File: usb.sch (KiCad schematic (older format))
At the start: 7 parts, among them U23 FT313HL-LQFP64-0.5

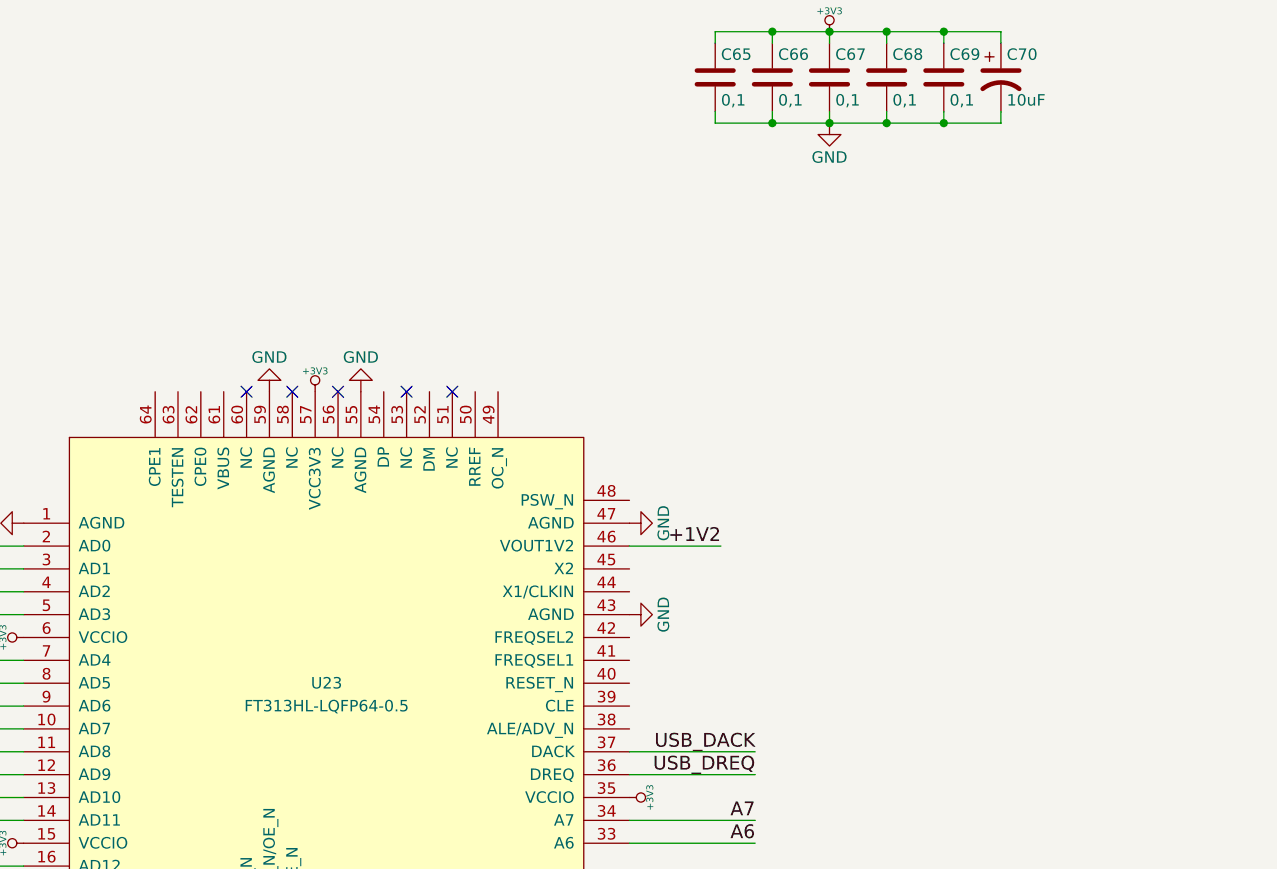
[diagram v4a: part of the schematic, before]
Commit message: Add USB connector
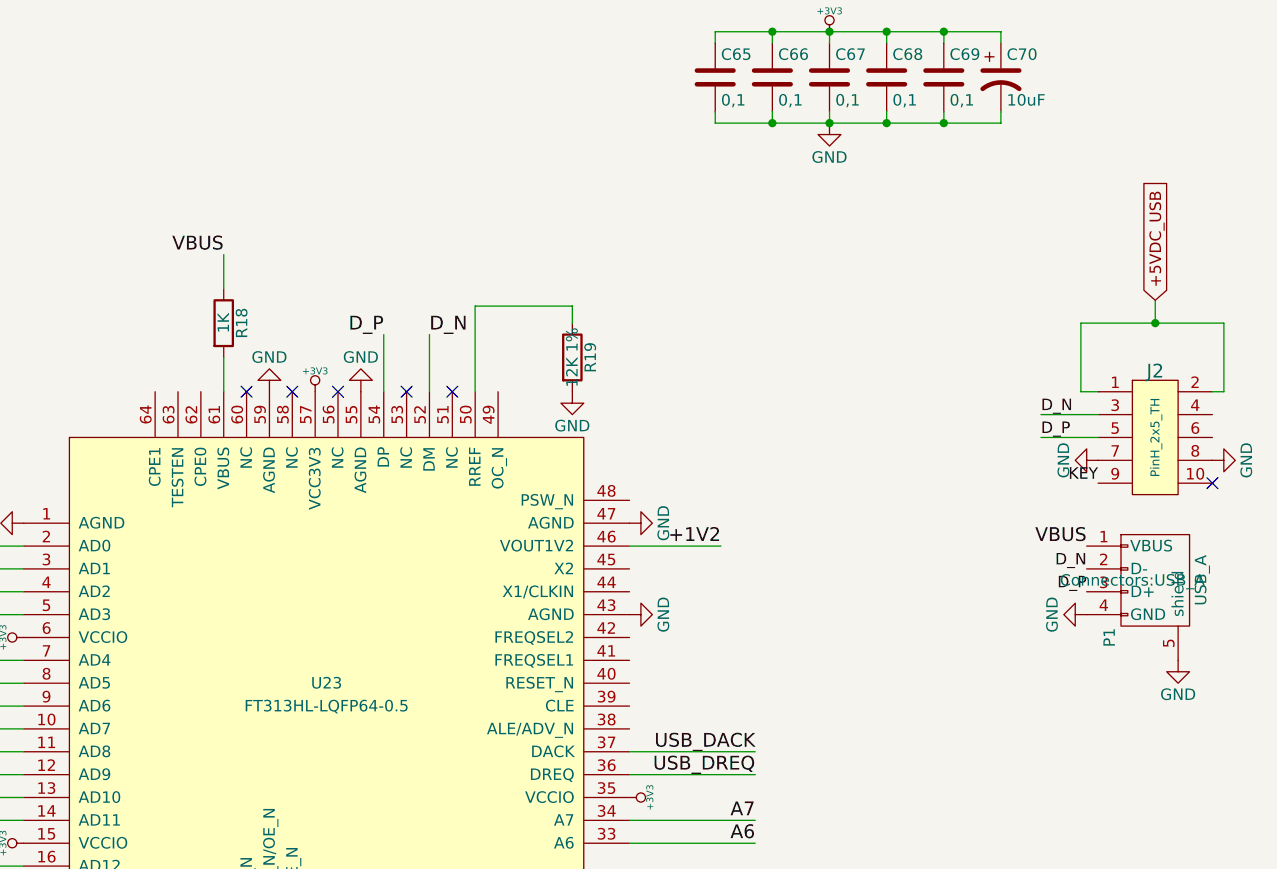
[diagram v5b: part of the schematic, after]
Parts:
- added J2: Pinheader_2x5_TH_WALL, Pin_Headers:Pin_Header_Straight_2x05_Pitch2.54mm, symbol Pinheader_2x5_TH_WALL
- added P1: USB_A, Connectors:USB_A, symbol USB_A
- added R18: 1K, symbol R
- added R19: 12K 1%, symbol R
- C65, C66, C67, C68, C69: footprint (none) -> Capacitors_SMD:C_0603
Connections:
- net labels added: +5VDC_USB, D_N, D_P, KEY, VBUS
- wire segments 77 -> 92
- no-connect marks 5 -> 6
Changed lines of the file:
@@
 $EndComp
 $Comp
-L GND #PWR147
+L GND #PWR148
 U 1 1 587F942A
 P 7000 3425
-F 0 "#PWR147" H 7000 3175 50  0001 C CNN
+F 0 "#PWR148" H 7000 3175 50  0001 C CNN
 F 1 "GND" H 7000 3275 50  0000 C CNN
 F 2 "" H 7000 3425 50  0000 C CNN
@@
 $EndComp
 $Comp
-L GND #PWR146
+L GND #PWR147
 U 1 1 587F944F
 P 7000 3025
-F 0 "#PWR146" H 7000 2775 50  0001 C CNN
+F 0 "#PWR147" H 7000 2775 50  0001 C CNN
 F 1 "GND" H 7000 2875 50  0000 C CNN
 F 2 "" H 7000 3025 50  0000 C CNN
@@
 $EndComp
 $Comp
-L +3V3 #PWR149
+L +3V3 #PWR150
 U 1 1 587FA4A0
 P 7875 875
-F 0 "#PWR149" H 7975 925 20  0001 C CNN
+F 0 "#PWR150" H 7975 925 20  0001 C CNN
 F 1 "+3V3" H 7875 965 30  0000 C CNN
 F 2 "" H 7875 875 60  0000 C CNN
@@
 F 0 "C65" H 7400 1175 50  0000 L CNN
 F 1 "0,1" H 7400 975 50  0000 L CNN
-F 2 "" H 7413 925 50  0001 C CNN
+F 2 "Capacitors_SMD:C_0603" H 7413 925 50  0001 C CNN
 F 3 "" H 7375 1075 50  0000 C CNN
 	1    7375 1075
@@
 F 0 "C66" H 7650 1175 50  0000 L CNN
 F 1 "0,1" H 7650 975 50  0000 L CNN
-F 2 "" H 7663 925 50  0001 C CNN
+F 2 "Capacitors_SMD:C_0603" H 7663 925 50  0001 C CNN
 F 3 "" H 7625 1075 50  0000 C CNN
 	1    7625 1075
@@
 F 0 "C67" H 7900 1175 50  0000 L CNN
 F 1 "0,1" H 7900 975 50  0000 L CNN
-F 2 "" H 7913 925 50  0001 C CNN
+F 2 "Capacitors_SMD:C_0603" H 7913 925 50  0001 C CNN
 F 3 "" H 7875 1075 50  0000 C CNN
 	1    7875 1075
@@
 F 0 "C68" H 8150 1175 50  0000 L CNN
 F 1 "0,1" H 8150 975 50  0000 L CNN
-F 2 "" H 8163 925 50  0001 C CNN
+F 2 "Capacitors_SMD:C_0603" H 8163 925 50  0001 C CNN
 F 3 "" H 8125 1075 50  0000 C CNN
 	1    8125 1075
@@
 $EndComp
 $Comp
-L GND #PWR150
+L GND #PWR151
 U 1 1 587FA6CC
 P 7875 1275
-F 0 "#PWR150" H 7875 1025 50  0001 C CNN
+F 0 "#PWR151" H 7875 1025 50  0001 C CNN
 F 1 "GND" H 7875 1125 50  0000 C CNN
 F 2 "" H 7875 1275 50  0000 C CNN
@@
 $EndComp
 $Comp
-L +3V3 #PWR148
+L +3V3 #PWR149
 U 1 1 587FB222
 P 7000 4225
-F 0 "#PWR148" H 7100 4275 20  0001 C CNN
+F 0 "#PWR149" H 7100 4275 20  0001 C CNN
 F 1 "+3V3" H 7000 4315 30  0000 C CNN
 F 2 "" H 7000 4225 60  0000 C CNN
@@
 F 0 "C69" H 8400 1175 50  0000 L CNN
 F 1 "0,1" H 8400 975 50  0000 L CNN
-F 2 "" H 8413 925 50  0001 C CNN
+F 2 "Capacitors_SMD:C_0603" H 8413 925 50  0001 C CNN
 F 3 "" H 8375 1075 50  0000 C CNN
 	1    8375 1075
@@
 Text HLabel 1575 5325 0    60   BiDi ~ 0
 USB_DREQ
+$Comp
+L Pinheader_2x5_TH_WALL J2
+U 1 1 588FAD1B
+P 9300 2800
+F 0 "J2" H 9300 3240 60  0000 C CNN
+F 1 "Pinheader_2x5_TH_WALL" H 9270 3330 60  0001 C CNN
+F 2 "Pin_Headers:Pin_Header_Straight_2x05_Pitch2.54mm" H 9280 3430 60  0001 C CNN
+F 3 "" H 9300 2900 60  0000 C CNN
+F 4 "S9169-ND" H 9320 3900 60  0001 C CNN "Vendor Part Number"
+F 5 "SBH11-PBPC-D05-ST-BK" H 9250 3610 60  0001 C CNN "Manufacturer Part Number"
+F 6 "CONN HEADER, 2.54MM, 10POS, GOLD," H 9350 3520 60  0001 C CNN "Description"
+F 7 "Digi-Key" H 9280 3800 60  0001 C CNN "Vendor"
+F 8 "Sullins Connector Solutions" H 9260 3710 60  0001 C CNN "Manufacturer"
+F 9 "PinH_2x5_TH" V 9300 2950 39  0000 C CNN "Component Value"
+	1    9300 2800
+	1    0    0    -1
+$EndComp
+$Comp
+L GND #PWR155
+U 1 1 588FAE50
+P 9550 2750
+F 0 "#PWR155" H 9550 2500 50  0001 C CNN
+F 1 "GND" H 9550 2600 50  0000 C CNN
+F 2 "" H 9550 2750 50  0000 C CNN
+F 3 "" H 9550 2750 50  0000 C CNN
+	1    9550 2750
+	0    -1   -1   0
+$EndComp
+$Comp
+L GND #PWR153
+U 1 1 588FAEAB
+P 9050 2750
+F 0 "#PWR153" H 9050 2500 50  0001 C CNN
+F 1 "GND" H 9050 2600 50  0000 C CNN
+F 2 "" H 9050 2750 50  0000 C CNN
+F 3 "" H 9050 2750 50  0000 C CNN
+	1    9050 2750
+	0    1    1    0
+$EndComp
+NoConn ~ 9550 2850
+Text Label 9050 2850 2    50   ~ 0
+KEY
+Text GLabel 9300 2050 1    50   Input ~ 0
++5VDC_USB
+Wire Wire Line
+	9300 2050 9300 2150
+Wire Wire Line
+	8975 2150 9600 2150
+Wire Wire Line
+	8975 2150 8975 2450
+Wire Wire Line
+	8975 2450 9050 2450
+Wire Wire Line
+	9600 2150 9600 2450
+Wire Wire Line
+	9600 2450 9550 2450
+Connection ~ 9300 2150
+Wire Wire Line
+	9050 2550 8800 2550
+Wire Wire Line
+	9050 2650 8800 2650
+Text Label 8800 2550 0    50   ~ 0
+D_N
+Text Label 8800 2650 0    50   ~ 0
+D_P
+Wire Wire Line
+	5925 2450 5925 2200
+Wire Wire Line
+	6125 2450 6125 2200
+Text Label 5925 2200 2    60   ~ 0
+D_P
+Text Label 6125 2200 0    60   ~ 0
+D_N
+$Comp
+L R R19
+U 1 1 588FBE83
+P 6750 2300
+F 0 "R19" V 6830 2300 50  0000 C CNN
+F 1 "12K 1%" V 6750 2300 50  0000 C CNN
+F 2 "" V 6680 2300 50  0000 C CNN
+F 3 "" H 6750 2300 50  0000 C CNN
+	1    6750 2300
+	1    0    0    -1
+$EndComp
+Wire Wire Line
+	6325 2450 6325 2075
+Wire Wire Line
+	6325 2075 6750 2075
+Wire Wire Line
+	6750 2075 6750 2150
+$Comp
+L GND #PWR146
+U 1 1 588FBF68
+P 6750 2450
+F 0 "#PWR146" H 6750 2200 50  0001 C CNN
+F 1 "GND" H 6750 2300 50  0000 C CNN
+F 2 "" H 6750 2450 50  0000 C CNN
+F 3 "" H 6750 2450 50  0000 C CNN
+	1    6750 2450
+	1    0    0    -1
+$EndComp
+$Comp
+L R R18
+U 1 1 588FC74E
+P 5225 2150
+F 0 "R18" V 5305 2150 50  0000 C CNN
+F 1 "1K" V 5225 2150 50  0000 C CNN
+F 2 "" V 5155 2150 50  0000 C CNN
+F 3 "" H 5225 2150 50  0000 C CNN
+	1    5225 2150
+	1    0    0    -1
+$EndComp
+Wire Wire Line
+	5225 2300 5225 2450
+Wire Wire Line
+	5225 2000 5225 1850
+Text Label 5225 1850 2    60   ~ 0
+VBUS
+$Comp
+L USB_A P1
+U 1 1 588FD24C
+P 9300 3325
+F 0 "P1" H 9500 3125 50  0000 C CNN
+F 1 "USB_A" H 9250 3525 50  0000 C CNN
+F 2 "Connectors:USB_A" V 9250 3225 50  0000 C CNN
+F 3 "" V 9250 3225 50  0000 C CNN
+	1    9300 3325
+	0    1    1    0
+$EndComp
+Text Label 9000 3125 2    60   ~ 0
+VBUS
+Text Label 9000 3225 2    50   ~ 0
+D_N
+Text Label 9000 3325 2    50   ~ 0
+D_P
+$Comp
+L GND #PWR152
+U 1 1 588FD418
+P 9000 3425
+F 0 "#PWR152" H 9000 3175 50  0001 C CNN
+F 1 "GND" H 9000 3275 50  0000 C CNN
+F 2 "" H 9000 3425 50  0000 C CNN
+F 3 "" H 9000 3425 50  0000 C CNN
+	1    9000 3425
+	0    1    1    0
+$EndComp
+$Comp
+L GND #PWR154
+U 1 1 588FDBE9
+P 9400 3625
+F 0 "#PWR154" H 9400 3375 50  0001 C CNN
+F 1 "GND" H 9400 3475 50  0000 C CNN
+F 2 "" H 9400 3625 50  0000 C CNN
+F 3 "" H 9400 3625 50  0000 C CNN
+	1    9400 3625
+	1    0    0    -1
+$EndComp
 $EndSCHEMATC

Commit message: More USB stuff
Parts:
- removed J2: Pinheader_2x5_TH_WALL, Pin_Headers:Pin_Header_Straight_2x05_Pitch2.54mm, symbol Pinheader_2x5_TH_WALL
- added C108: 0,1, Capacitors_SMD:C_0603, symbol C
- added C109: 22uF, Capacitors_Tantalum_SMD:CP_Tantalum_Case-B_EIA-3528-21_Wave, symbol CP1
- added C110, C111: 27pF, Capacitors_SMD:C_0603, symbol C
- added R20, R22, R23, R25: 000, Resistors_SMD:R_0603, symbol R
- added R21, R24: 10K, Resistors_SMD:R_0603, symbol R
- added U25: TPS2024D, Housings_SOIC:SOIC-8_3.9x4.9mm_Pitch1.27mm, symbol TPS2024D
- added Y2: Geyer_KX7_12MHz, Crystals:Crystal_SMD_3225-4pin_3.2x2.5mm, symbol Crystal_GND24
- R18, R19: footprint (none) -> Resistors_SMD:R_0603
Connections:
- net labels added: +5VDC, CPE0, CPE1, OC_N, USB_NRESET, nEN
- net labels removed: +5VDC_USB, KEY
- wire segments 92 -> 121
- no-connect marks 6 -> 5
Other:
- note added: "TESTEN: internal pulldown.\nFor normal operation leave floating."
- moved on the sheet: C65, C66, C67, C68, C69, C70, P1

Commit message: Up
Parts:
- added C112, C113, C114: 0,1, Capacitors_SMD:C_0603, symbol C
- added C115: 10uF, symbol CP1
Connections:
- wire segments 121 -> 131
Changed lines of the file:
@@
 NoConn ~ 5325 2450
 $Comp
-L GND #PWR139
+L GND #PWR152
 U 1 1 587F93F7
 P 4350 3025
-F 0 "#PWR139" H 4350 2775 50  0001 C CNN
+F 0 "#PWR152" H 4350 2775 50  0001 C CNN
 F 1 "GND" H 4350 2875 50  0000 C CNN
 F 2 "" H 4350 3025 50  0000 C CNN
@@
 $EndComp
 $Comp
-L GND #PWR148
+L GND #PWR157
 U 1 1 587F942A
 P 7000 3425
-F 0 "#PWR148" H 7000 3175 50  0001 C CNN
+F 0 "#PWR157" H 7000 3175 50  0001 C CNN
 F 1 "GND" H 7000 3275 50  0000 C CNN
 F 2 "" H 7000 3425 50  0000 C CNN
@@
 $EndComp
 $Comp
-L GND #PWR147
+L GND #PWR153
 U 1 1 587F944F
 P 7000 3025
-F 0 "#PWR147" H 7000 2775 50  0001 C CNN
+F 0 "#PWR153" H 7000 2775 50  0001 C CNN
 F 1 "GND" H 7000 2875 50  0000 C CNN
 F 2 "" H 7000 3025 50  0000 C CNN
@@
 $EndComp
 $Comp
-L GND #PWR145
+L GND #PWR148
 U 1 1 587F9489
 P 5825 2450
-F 0 "#PWR145" H 5825 2200 50  0001 C CNN
+F 0 "#PWR148" H 5825 2200 50  0001 C CNN
 F 1 "GND" H 5825 2300 50  0000 C CNN
 F 2 "" H 5825 2450 50  0000 C CNN
@@
 $EndComp
 $Comp
-L GND #PWR142
+L GND #PWR146
 U 1 1 587F9497
 P 5425 2450
-F 0 "#PWR142" H 5425 2200 50  0001 C CNN
+F 0 "#PWR146" H 5425 2200 50  0001 C CNN
 F 1 "GND" H 5425 2300 50  0000 C CNN
 F 2 "" H 5425 2450 50  0000 C CNN
@@
 $EndComp
 $Comp
-L +3V3 #PWR161
+L +3V3 #PWR139
 U 1 1 587FA4A0
 P 10100 825
-F 0 "#PWR161" H 10200 875 20  0001 C CNN
+F 0 "#PWR139" H 10200 875 20  0001 C CNN
 F 1 "+3V3" H 10100 915 30  0000 C CNN
 F 2 "" H 10100 825 60  0000 C CNN
@@
 $EndComp
 $Comp
-L GND #PWR162
+L GND #PWR141
 U 1 1 587FA6CC
 P 10100 1225
-F 0 "#PWR162" H 10100 975 50  0001 C CNN
+F 0 "#PWR141" H 10100 975 50  0001 C CNN
 F 1 "GND" H 10100 1075 50  0000 C CNN
 F 2 "" H 10100 1225 50  0000 C CNN
@@
 $EndComp
 $Comp
-L +3V3 #PWR140
+L +3V3 #PWR158
 U 1 1 587FB090
 P 4350 3525
-F 0 "#PWR140" H 4450 3575 20  0001 C CNN
+F 0 "#PWR158" H 4450 3575 20  0001 C CNN
 F 1 "+3V3" H 4350 3615 30  0000 C CNN
 F 2 "" H 4350 3525 60  0000 C CNN
@@
 $EndComp
 $Comp
-L +3V3 #PWR144
+L +3V3 #PWR166
 U 1 1 587FB177
 P 5725 5100
-F 0 "#PWR144" H 5825 5150 20  0001 C CNN
+F 0 "#PWR166" H 5825 5150 20  0001 C CNN
 F 1 "+3V3" H 5725 5190 30  0000 C CNN
 F 2 "" H 5725 5100 60  0000 C CNN
@@
 $EndComp
 $Comp
-L +3V3 #PWR149
+L +3V3 #PWR164
 U 1 1 587FB222
 P 7000 4225
-F 0 "#PWR149" H 7100 4275 20  0001 C CNN
+F 0 "#PWR164" H 7100 4275 20  0001 C CNN
 F 1 "+3V3" H 7000 4315 30  0000 C CNN
 F 2 "" H 7000 4225 60  0000 C CNN
@@
 $EndComp
 $Comp
-L +3V3 #PWR141
+L +3V3 #PWR165
 U 1 1 587FB43F
 P 4350 4425
-F 0 "#PWR141" H 4450 4475 20  0001 C CNN
+F 0 "#PWR165" H 4450 4475 20  0001 C CNN
 F 1 "+3V3" H 4350 4515 30  0000 C CNN
 F 2 "" H 4350 4425 60  0000 C CNN
@@
 +1V2
 $Comp
-L +3V3 #PWR143
+L +3V3 #PWR147
 U 1 1 587FFC16
 P 5625 2450
-F 0 "#PWR143" H 5725 2500 20  0001 C CNN
+F 0 "#PWR147" H 5725 2500 20  0001 C CNN
 F 1 "+3V3" H 5625 2540 30  0000 C CNN
 F 2 "" H 5625 2450 60  0000 C CNN
@@
 Text Label 7550 4025 2    60   ~ 0
 USB_DACK
-Text Label 2125 5325 2    60   ~ 0
+Text Label 2175 5025 2    60   ~ 0
 USB_DREQ
-Text Label 2125 5225 2    60   ~ 0
+Text Label 2175 4925 2    60   ~ 0
 USB_DACK
-Text HLabel 1575 5225 0    60   BiDi ~ 0
+Text HLabel 1625 4925 0    60   BiDi ~ 0
 USB_DACK
-Text HLabel 1575 5325 0    60   BiDi ~ 0
+Text HLabel 1625 5025 0    60   BiDi ~ 0
 USB_DREQ
 Text Label 5925 2200 2    60   ~ 0
@@
 $EndComp
 $Comp
-L GND #PWR146
+L GND #PWR149
 U 1 1 588FBF68
 P 6750 2450
-F 0 "#PWR146" H 6750 2200 50  0001 C CNN
+F 0 "#PWR149" H 6750 2200 50  0001 C CNN
 F 1 "GND" H 6750 2300 50  0000 C CNN
 F 2 "" H 6750 2450 50  0000 C CNN
@@
 D_P
 $Comp
-L GND #PWR163
+L GND #PWR160
 U 1 1 588FD418
 P 10200 3850
-F 0 "#PWR163" H 10200 3600 50  0001 C CNN
+F 0 "#PWR160" H 10200 3600 50  0001 C CNN
 F 1 "GND" H 10200 3700 50  0000 C CNN
 F 2 "" H 10200 3850 50  0000 C CNN
@@
 $EndComp
 $Comp
-L GND #PWR164
+L GND #PWR163
 U 1 1 588FDBE9
 P 10600 4050
-F 0 "#PWR164" H 10600 3800 50  0001 C CNN
+F 0 "#PWR163" H 10600 3800 50  0001 C CNN
 F 1 "GND" H 10600 3900 50  0000 C CNN
 F 2 "" H 10600 4050 50  0000 C CNN
@@
 $EndComp
 $Comp
-L GND #PWR155
+L GND #PWR145
 U 1 1 5890EDC6
 P 8700 1825
-F 0 "#PWR155" H 8700 1575 50  0001 C CNN
+F 0 "#PWR145" H 8700 1575 50  0001 C CNN
 F 1 "GND" H 8700 1675 50  0000 C CNN
 F 2 "" H 8700 1825 50  0000 C CNN
@@
 $EndComp
 $Comp
-L GND #PWR153
+L GND #PWR150
 U 1 1 5890F077
 P 8175 2500
-F 0 "#PWR153" H 8175 2250 50  0001 C CNN
+F 0 "#PWR150" H 8175 2250 50  0001 C CNN
 F 1 "GND" H 8175 2350 50  0000 C CNN
 F 2 "" H 8175 2500 50  0000 C CNN
@@
 $EndComp
 $Comp
-L +3V3 #PWR150
+L +3V3 #PWR142
 U 1 1 589100DF
 P 7775 1625
-F 0 "#PWR150" H 7875 1675 20  0001 C CNN
+F 0 "#PWR142" H 7875 1675 20  0001 C CNN
 F 1 "+3V3" H 7775 1715 30  0000 C CNN
 F 2 "" H 7775 1625 60  0000 C CNN
@@
 $EndComp
 $Comp
-L +5VDC #PWR152
+L +5VDC #PWR143
 U 1 1 58911317
 P 8175 1625
-F 0 "#PWR152" H 8275 1675 20  0001 C CNN
+F 0 "#PWR143" H 8275 1675 20  0001 C CNN
 F 1 "+5VDC" H 8175 1715 30  0000 C CNN
 F 2 "" H 8175 1625 60  0000 C CNN
@@
 	7000 4025 7550 4025
 Wire Wire Line
-	1575 5325 2125 5325
-Wire Wire Line
-	1575 5225 2125 5225
+	1625 5025 2175 5025
+Wire Wire Line
+	1625 4925 2175 4925
 Wire Wire Line
 	5925 2450 5925 2200
@@
 	8100 3625 7000 3625
 $Comp
-L GND #PWR151
+L GND #PWR161
 U 1 1 58918521
 P 8100 4025
-F 0 "#PWR151" H 8100 3775 50  0001 C CNN
+F 0 "#PWR161" H 8100 3775 50  0001 C CNN
 F 1 "GND" H 8100 3875 50  0000 C CNN
 F 2 "" H 8100 4025 50  0000 C CNN
@@
 $EndComp
 $Comp
-L GND #PWR154
+L GND #PWR162
 U 1 1 58918565
 P 8275 4025
-F 0 "#PWR154" H 8275 3775 50  0001 C CNN
+F 0 "#PWR162" H 8275 3775 50  0001 C CNN
 F 1 "GND" H 8275 3875 50  0000 C CNN
 F 2 "" H 8275 4025 50  0000 C CNN
@@
 $EndComp
 $Comp
-L +3V3 #PWR160
+L +3V3 #PWR144
 U 1 1 58919A0E
 P 9800 1625
-F 0 "#PWR160" H 9900 1675 20  0001 C CNN
+F 0 "#PWR144" H 9900 1675 20  0001 C CNN
 F 1 "+3V3" H 9800 1715 30  0000 C CNN
 F 2 "" H 9800 1625 60  0000 C CNN
@@
 $EndComp
 $Comp
-L GND #PWR165
+L GND #PWR154
 U 1 1 5891AE93
 P 10650 3125
-F 0 "#PWR165" H 10650 2875 50  0001 C CNN
+F 0 "#PWR154" H 10650 2875 50  0001 C CNN
 F 1 "GND" H 10650 2975 50  0000 C CNN
 F 2 "" H 10650 3125 50  0000 C CNN
@@
 	8750 3475 8950 3475
 $Comp
-L GND #PWR156
+L GND #PWR155
 U 1 1 5891C617
 P 8800 3275
-F 0 "#PWR156" H 8800 3025 50  0001 C CNN
+F 0 "#PWR155" H 8800 3025 50  0001 C CNN
 F 1 "GND" H 8800 3125 50  0000 C CNN
 F 2 "" H 8800 3275 50  0000 C CNN
@@
 $EndComp
 $Comp
-L GND #PWR159
+L GND #PWR156
 U 1 1 5891C65E
 P 9100 3275
-F 0 "#PWR159" H 9100 3025 50  0001 C CNN
+F 0 "#PWR156" H 9100 3025 50  0001 C CNN
 F 1 "GND" H 9100 3125 50  0000 C CNN
 F 2 "" H 9100 3275 50  0000 C CNN
@@
 Connection ~ 8850 3075
 $Comp
-L GND #PWR158
+L GND #PWR159
 U 1 1 5891DDB7
 P 8850 3850
-F 0 "#PWR158" H 8850 3600 50  0001 C CNN
+F 0 "#PWR159" H 8850 3600 50  0001 C CNN
 F 1 "GND" H 8850 3700 50  0000 C CNN
 F 2 "" H 8850 3850 50  0000 C CNN
@@
 $EndComp
 $Comp
-L GND #PWR157
+L GND #PWR151
 U 1 1 5891DE04
 P 8850 2700
-F 0 "#PWR157" H 8850 2450 50  0001 C CNN
+F 0 "#PWR151" H 8850 2450 50  0001 C CNN
 F 1 "GND" H 8850 2550 50  0000 C CNN
 F 2 "" H 8850 2700 50  0000 C CNN
@@
 	-1   0    0    1
 $EndComp
+Text Label 6175 850  2    60   ~ 0
++1V2
+Wire Wire Line
+	6175 850  7150 850
+$Comp
+L C C112
+U 1 1 58A75D0F
+P 6350 1050
+F 0 "C112" H 6375 1150 50  0000 L CNN
+F 1 "0,1" H 6375 950 50  0000 L CNN
+F 2 "Capacitors_SMD:C_0603" H 6388 900 50  0001 C CNN
+F 3 "" H 6350 1050 50  0000 C CNN
+	1    6350 1050
+	1    0    0    -1
+$EndComp
+$Comp
+L C C113
+U 1 1 58A75EF9
+P 6625 1050
+F 0 "C113" H 6650 1150 50  0000 L CNN
+F 1 "0,1" H 6650 950 50  0000 L CNN
+F 2 "Capacitors_SMD:C_0603" H 6663 900 50  0001 C CNN
+F 3 "" H 6625 1050 50  0000 C CNN
+	1    6625 1050
+	1    0    0    -1
+$EndComp
+$Comp
+L C C114
+U 1 1 58A75F69
+P 6875 1050
+F 0 "C114" H 6900 1150 50  0000 L CNN
+F 1 "0,1" H 6900 950 50  0000 L CNN
+F 2 "Capacitors_SMD:C_0603" H 6913 900 50  0001 C CNN
+F 3 "" H 6875 1050 50  0000 C CNN
+	1    6875 1050
+	1    0    0    -1
+$EndComp
+Wire Wire Line
+	6350 1225 7150 1225
+Wire Wire Line
+	6350 1200 6350 1225
+Wire Wire Line
+	6350 900  6350 850
+Connection ~ 6350 850
+Wire Wire Line
+	6625 900  6625 850
+Connection ~ 6625 850
+Wire Wire Line
+	6875 900  6875 850
+Connection ~ 6875 850
+Wire Wire Line
+	6625 1200 6625 1225
+Connection ~ 6625 1225
+Wire Wire Line
+	6875 1200 6875 1225
+Connection ~ 6875 1225
+$Comp
+L GND #PWR140
+U 1 1 58A7680E
+P 6625 1225
+F 0 "#PWR140" H 6625 975 50  0001 C CNN
+F 1 "GND" H 6625 1075 50  0000 C CNN
+F 2 "" H 6625 1225 50  0000 C CNN
+F 3 "" H 6625 1225 50  0000 C CNN
+	1    6625 1225
+	1    0    0    -1
+$EndComp
+$Comp
+L CP1 C115
+U 1 1 58A769C2
+P 7150 1050
+F 0 "C115" H 7175 1150 50  0000 L CNN
+F 1 "10uF" H 7175 950 50  0000 L CNN
+F 2 "" H 7150 1050 50  0001 C CNN
+F 3 "" H 7150 1050 50  0000 C CNN
+	1    7150 1050
+	1    0    0    -1
+$EndComp
+Wire Wire Line
+	7150 850  7150 900
+Wire Wire Line
+	7150 1225 7150 1200
 $EndSCHEMATC

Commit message: A bit of routing
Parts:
- added IC1: EP4CE10F17, 256FBGA, symbol EP4CE10F17
- C109: footprint Capacitors_Tantalum_SMD:CP_Tantalum_Case-B_EIA-3528-21_Wave -> Capacitors_Tantalum_SMD:CP_Tantalum_Case-C_EIA-6032-28_Reflow
- C115, C70: footprint (none) -> Capacitors_Tantalum_SMD:CP_Tantalum_Case-B_EIA-3528-21_Reflow
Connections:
- net labels added: CONF_DONE, ETHSD0, ETHSD1, ETHSD10, ETHSD11, ETHSD12, ETHSD13, ETHSD14, ETHSD15, ETHSD2, ETHSD3, ETHSD4, ETHSD5, ETHSD6, ETHSD7, ETHSD8, ETHSD9, MSEL0, MSEL1, MSEL2
- net labels removed: AD0, AD1, AD10, AD11, AD12, AD13, AD14, AD15, AD2, AD3, AD4, AD5, AD6, AD7, AD8, AD9, USBAD[0:15], USBA[0:7]
- wire segments 131 -> 85
